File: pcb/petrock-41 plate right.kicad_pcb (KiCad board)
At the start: 2 copper layers, 119.3 x 87.9 mm, 20 parts, among them SW1 SW_PUSH, SW10 SW_PUSH, SW11 SW_PUSH, SW12 SW_PUSH, SW13 SW_PUSH, SW14 SW_PUSH, SW15 SW_PUSH, SW16 SW_PUSH, SW17 SW_PUSH, SW18 SW_PUSH, SW19 SW_PUSH, SW2 SW_PUSH, SW20 SW_PUSH, SW3 SW_PUSH, SW4 SW_PUSH, SW5 SW_PUSH, SW6 SW_PUSH, SW7 SW_PUSH, SW8 SW_PUSH, SW9 SW_PUSH

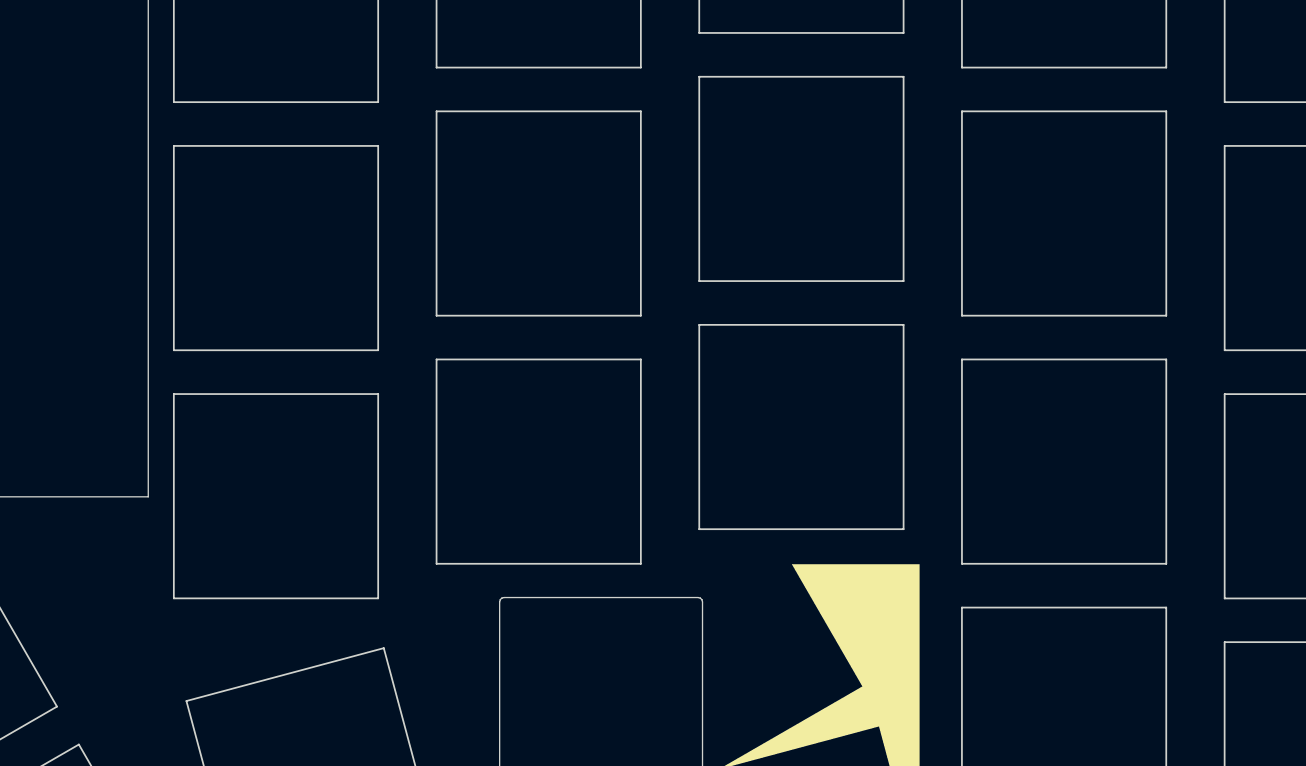
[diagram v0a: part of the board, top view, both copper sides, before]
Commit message: Standoffs in a rectangle, screw holes back in the switch plate
The standoff stack is holykeebs': a spacer through the main board's 3.1 mm
hole, a top screw through the switch plate, a bottom screw through the
bottom plate; the main board hangs from the switches. The plate's screw
holes, removed early on as supposed OLED-cover holes, are back (2.1 mm)
over every standoff.

Per half, four standoffs sit at four-key centres forming a 54 x 34 mm
rectangle (pinky|ring and index|inner index, top and bottom) and one at
the thumbs. The logo's standoff moves to the index bottom, so the logo
carries a solid 7 mm dot on board and plate. README: hardware (5 mm round
spacers; small-head top screws where four keys meet), assembly and feet.
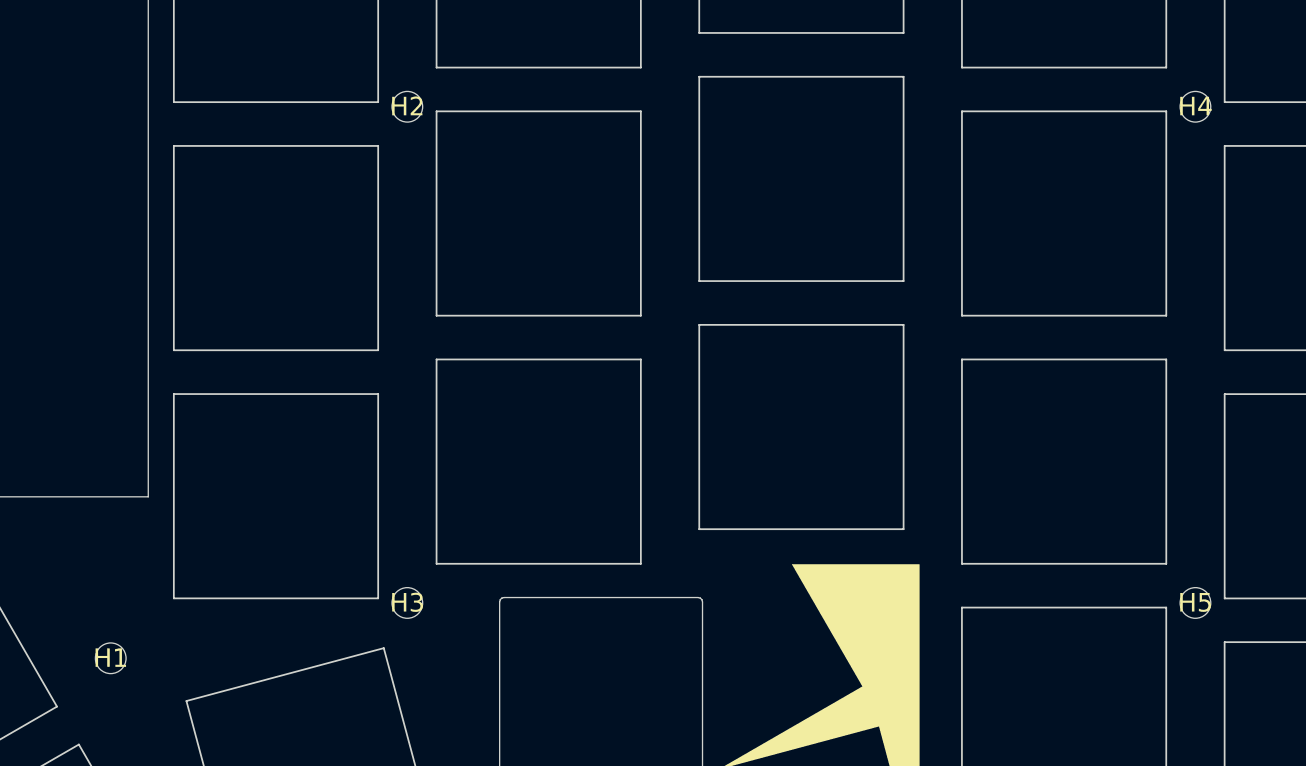
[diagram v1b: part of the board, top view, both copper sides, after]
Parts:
- added H1: , , F.Cu at (167.5, 111.0)
- added H2: , , F.Cu at (187.8, 73.2)
- added H3: , , F.Cu at (187.8, 107.2)
- added H4: , , F.Cu at (241.8, 73.2)
- added H5: , , F.Cu at (241.8, 107.2)

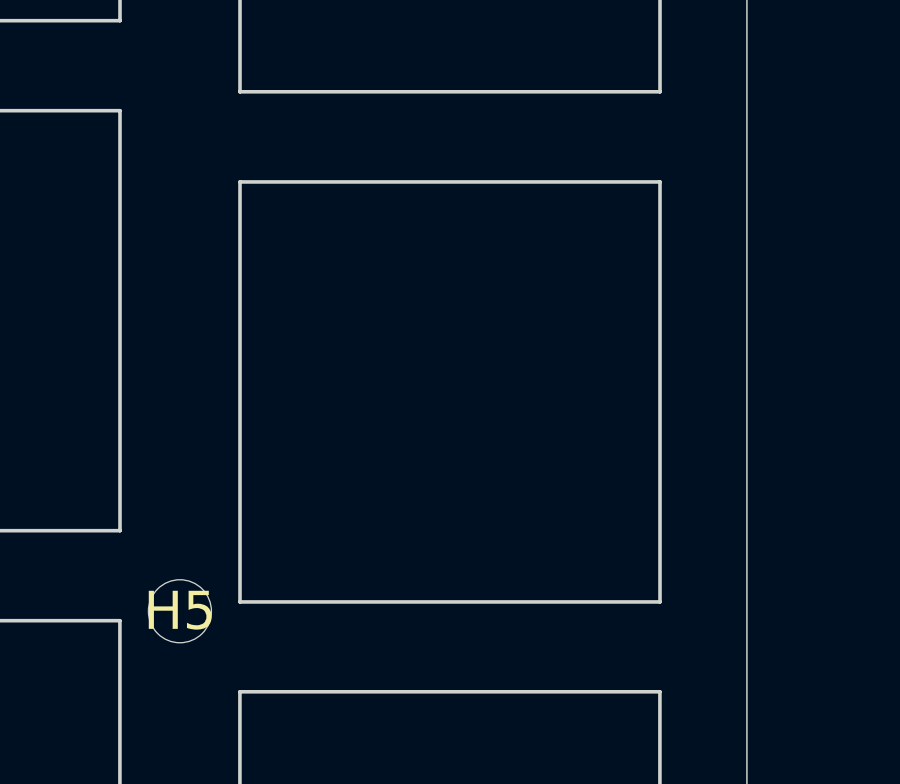
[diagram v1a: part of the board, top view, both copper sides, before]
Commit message: Boards, plates and renders built from 06b7685 (the hash printed on the boards)
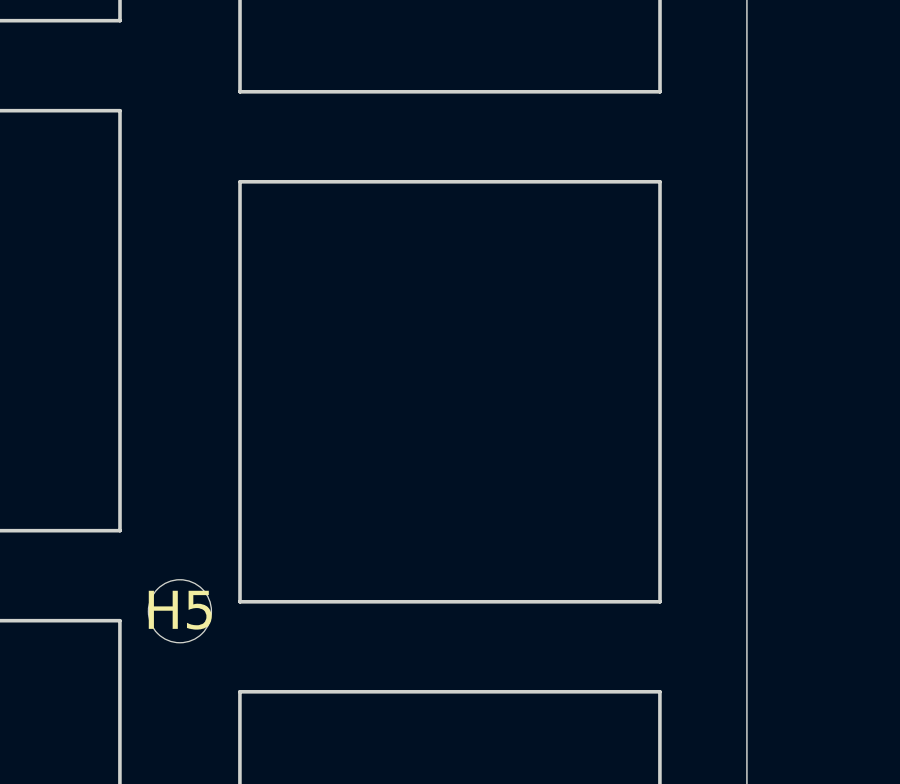
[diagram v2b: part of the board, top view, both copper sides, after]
